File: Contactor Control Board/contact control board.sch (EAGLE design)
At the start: 29 parts, among them K1 DS2Y-S-DC5V, Q1 2n2222, Q3 2n2222, Q4 MOSFET-NCHANNELFQP30N06L, U1 LM393AN

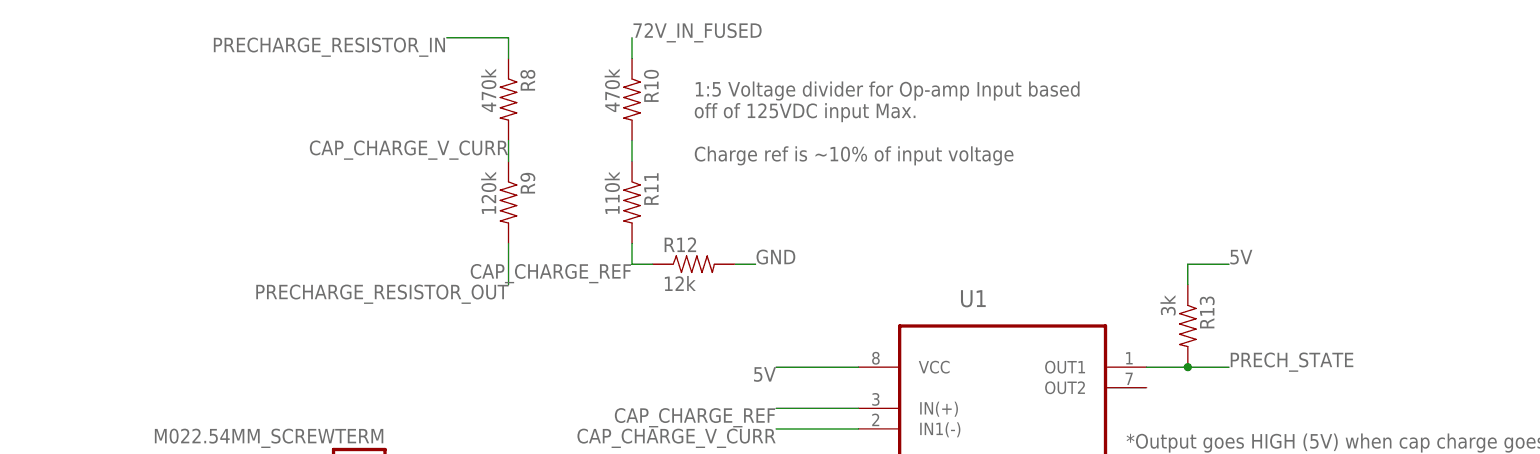
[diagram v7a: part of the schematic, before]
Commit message: Redoing voltage dividers so that they produce voltages on the oeprational range of our voltage comparator. Also re-wired the voltage
monitor for the capacitors to use capacitor voltage and not the voltage
over the pre-charge resistors.
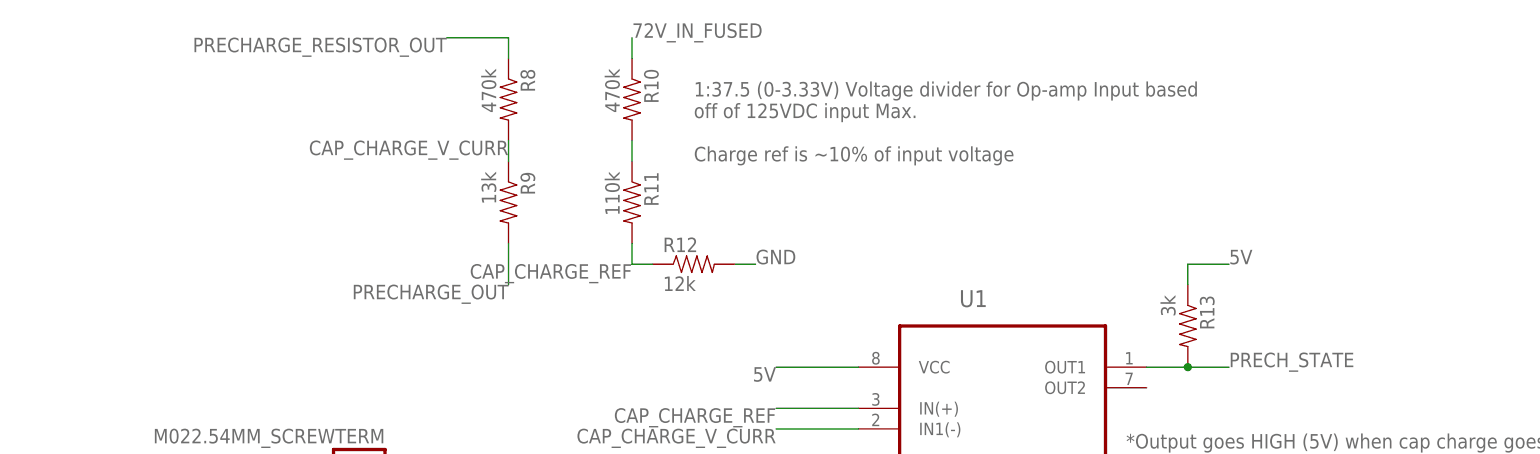
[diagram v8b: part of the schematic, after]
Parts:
- R9: value 120k -> 13k
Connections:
- net PRECHARGE_OUT: now also R9.2
- net PRECHARGE_RESISTOR_IN: no longer R8.1
- net PRECHARGE_RESISTOR_OUT: now also R8.1; no longer R9.2
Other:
- note added: "1:37.5 (0-3.33V) Voltage divider for Op-amp Input based off of 125VDC input Max. Charge ref is ~10% of input voltage"
- note removed: "1:5 Voltage divider for Op-amp Input based off of 125VDC input Max. Charge ref is ~10% of input voltage"
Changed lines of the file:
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@@
 <part name="RESISTOR" library="SparkFun-Connectors" deviceset="M02" device="2.54MM_SCREWTERM"/>
 <part name="R8" library="SparkFun-Resistors" deviceset="RESISTOR" device="PTH-1/4W" value="470k"/>
-<part name="R9" library="SparkFun-Resistors" deviceset="RESISTOR" device="PTH-1/4W" value="120k"/>
+<part name="R9" library="SparkFun-Resistors" deviceset="RESISTOR" device="PTH-1/4W" value="13k"/>
 <part name="R10" library="SparkFun-Resistors" deviceset="RESISTOR" device="PTH-1/4W" value="470k"/>
 <part name="R11" library="SparkFun-Resistors" deviceset="RESISTOR" device="PTH-1/4W" value="110k"/>
@@
 <sheet>
 <plain>
-<text x="93.98" y="152.4" size="1.778" layer="95">1:5 Voltage divider for Op-amp Input based
+<text x="93.98" y="152.4" size="1.778" layer="95">1:37.5 (0-3.33V) Voltage divider for Op-amp Input based
 off of 125VDC input Max.
 Charge ref is ~10% of input voltage</text>
@@
 <label x="2.54" y="7.62" size="1.778" layer="95" rot="R180"/>
 </segment>
+<segment>
+<pinref part="R9" gate="G$1" pin="2"/>
+<wire x1="71.12" y1="142.24" x2="71.12" y2="137.16" width="0.2032" layer="91"/>
+<label x="71.12" y="137.16" size="1.778" layer="95" rot="R180"/>
+</segment>
 </net>
 <net name="N$9" class="0">
@@
 <label x="2.54" y="17.78" size="1.778" layer="95" rot="R180"/>
 </segment>
+</net>
+<net name="PRECHARGE_RESISTOR_OUT" class="0">
+<segment>
+<pinref part="RESISTOR" gate="G$1" pin="2"/>
+<wire x1="45.72" y1="111.76" x2="40.64" y2="111.76" width="0.2032" layer="91"/>
+<label x="40.64" y="111.76" size="1.778" layer="95" rot="R180"/>
+</segment>
+<segment>
+<pinref part="K1" gate="3" pin="P"/>
+<wire x1="12.7" y1="0" x2="12.7" y2="-2.54" width="0.2032" layer="91"/>
+<wire x1="12.7" y1="-2.54" x2="2.54" y2="-2.54" width="0.2032" layer="91"/>
+<label x="2.54" y="-2.54" size="1.778" layer="95" rot="R180"/>
+</segment>
 <segment>
 <pinref part="R8" gate="G$1" pin="1"/>
@@
 </segment>
 </net>
-<net name="PRECHARGE_RESISTOR_OUT" class="0">
-<segment>
-<pinref part="RESISTOR" gate="G$1" pin="2"/>
-<wire x1="45.72" y1="111.76" x2="40.64" y2="111.76" width="0.2032" layer="91"/>
-<label x="40.64" y="111.76" size="1.778" layer="95" rot="R180"/>
-</segment>
-<segment>
-<pinref part="K1" gate="3" pin="P"/>
-<wire x1="12.7" y1="0" x2="12.7" y2="-2.54" width="0.2032" layer="91"/>
-<wire x1="12.7" y1="-2.54" x2="2.54" y2="-2.54" width="0.2032" layer="91"/>
-<label x="2.54" y="-2.54" size="1.778" layer="95" rot="R180"/>
-</segment>
-<segment>
-<pinref part="R9" gate="G$1" pin="2"/>
-<wire x1="71.12" y1="142.24" x2="71.12" y2="137.16" width="0.2032" layer="91"/>
-<label x="71.12" y="137.16" size="1.778" layer="95" rot="R180"/>
-</segment>
-</net>
